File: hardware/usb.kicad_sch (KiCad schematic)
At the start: 16 parts, among them J2 USB_C_Receptacle_USB2.0, Q2 MMBT3904, Q3 MMBT3904, U7 SRV05-4, U8 CH340C

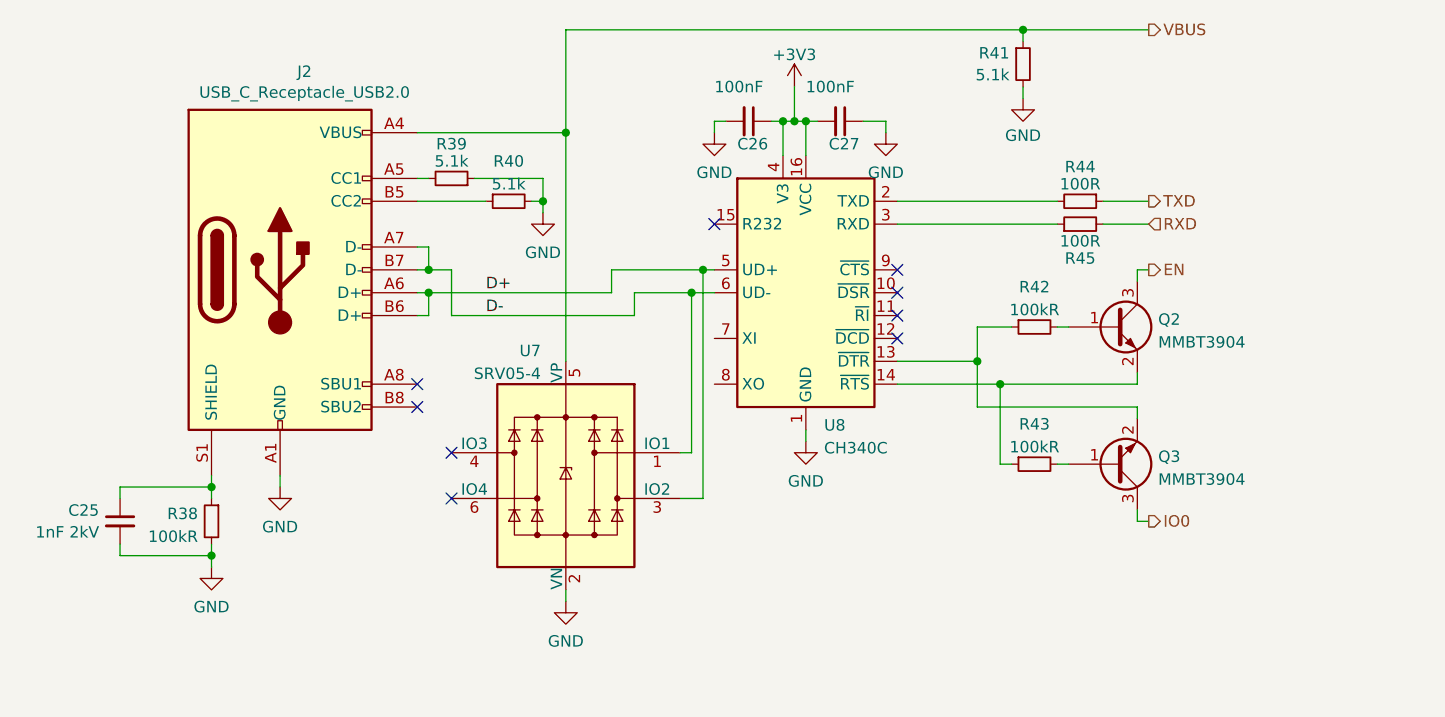
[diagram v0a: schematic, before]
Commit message: hardware: switch to ESP32-C3 MCU and Si3402-B for PoE
Further changes:
 - Enlarge center hole to 16mm diameter
 - Replace Ethernet Phy by KSZ8851 SPI MAC + Phy
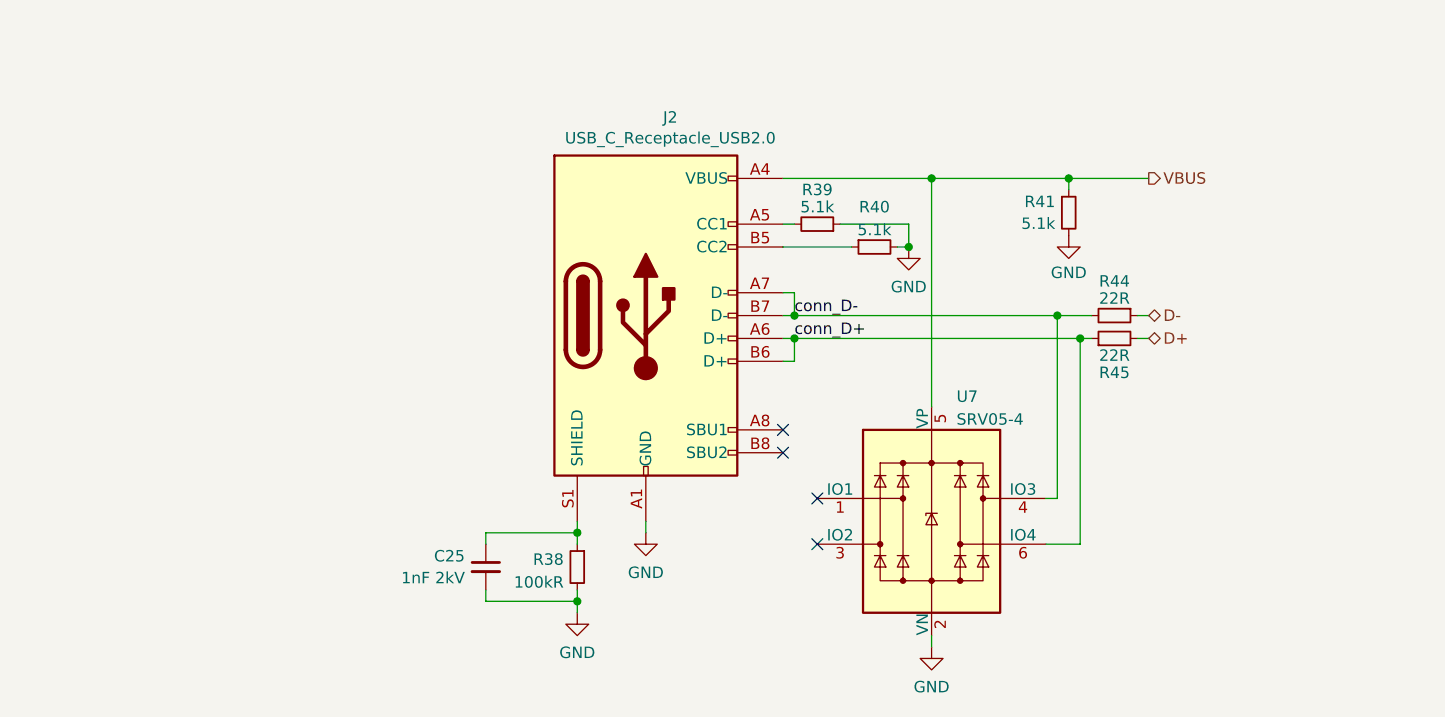
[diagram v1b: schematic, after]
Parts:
- removed C26, C27: 100nF, Capacitor_SMD:C_0402_1005Metric, symbol Device:C_Small
- removed Q2, Q3: MMBT3904, Package_TO_SOT_SMD:SOT-23, symbol Transistor_BJT:MMBT3904
- removed R42, R43: 100kR, Resistor_SMD:R_0402_1005Metric, symbol Device:R_Small
- removed U8: CH340C, Package_SO:SOIC-16_3.9x9.9mm_P1.27mm, symbol Interface_USB:CH340G
- R44, R45: value 100R -> 22R; LCSC C25076 -> C25092
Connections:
- net RXD is gone; now on net D+: R45.2
- net TXD is gone; now on net D-: R44.1
- net D+: no longer J2.A6 (D+), J2.B6 (D+), U7.3 (IO2)
- net D-: no longer J2.A7 (D-), J2.B7 (D-), U7.1 (IO1)
- net conn_D-: now reaches R44.2
- net conn_D-: now also J2.A7 (D-), J2.B7 (D-), U7.4 (IO3)
- net conn_D+: now reaches R45.1
- net conn_D+: now also J2.A6 (D+), J2.B6 (D+), U7.6 (IO4)
- no-connect marks 9 -> 4
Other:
- moved on the sheet: C25, J2, R38, R39, R40, R41, R44, R45, U7

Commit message: Implement review comments by Urmel
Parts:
- added C20, C21: 100nF, Capacitor_SMD:C_0402_1005Metric, symbol Device:C_Small
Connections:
- net GND: now also C20.2, C21.2
- new net +3V3: C20.1, C21.1

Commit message: rev 0.4 move button next to ethernet jack, kicad v9
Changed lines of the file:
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@@
 (kicad_sch
-	(version 20231120)
+	(version 20250114)
 	(generator "eeschema")
-	(generator_version "8.0")
+	(generator_version "9.0")
 	(paper "A4")
 	(junction
